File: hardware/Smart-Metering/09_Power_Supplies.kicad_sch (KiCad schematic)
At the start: 36 parts, among them J901 BATTERY_1S, SW901 POWER, U901 BQ24074RGT, U902 TPS63001, U903 TPS61089

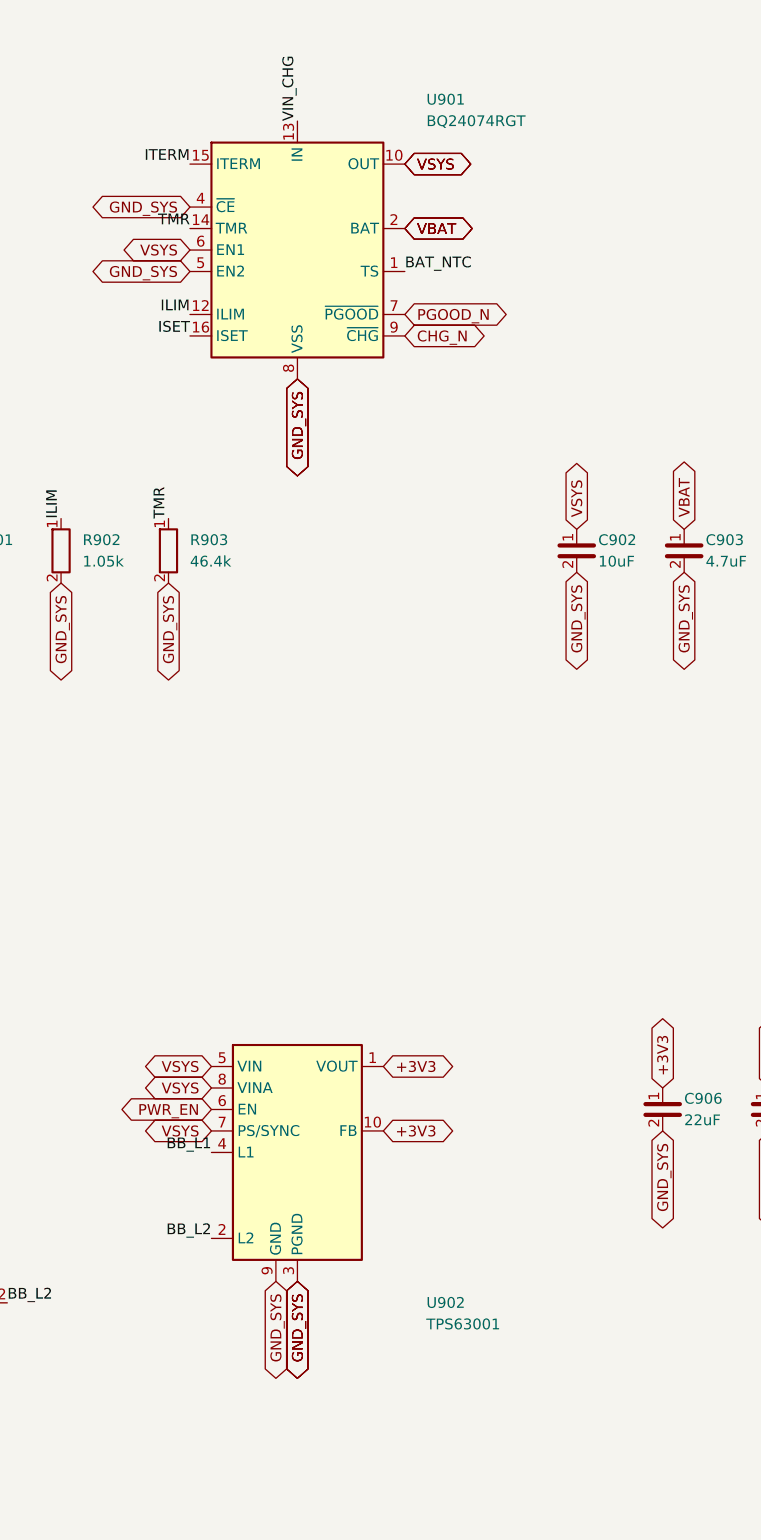
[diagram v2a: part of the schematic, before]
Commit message: Completa o esquemático: MCU, interface HMI e comunicações
05_Metrology_MCU: STM32F413RHT6 (símbolo oficial), mesma família da
plataforma de referência da biblioteca ADSW-PQ-CLS (NUCLEO-F413ZH).
SPI1 isolado para ADE9430/MCP3204, IRQ/DREADY/ZX em EXTI, CF1/CF2 em
timers, USART2 para a HMI, USART3 + DE para RS-485, USB FS, VBAT_SENSE,
estado do carregador, HSE 8 MHz, RTC com LSE 32,768 kHz e CR2032, SWD
de 10 pinos e LEDs de status e pulso.

07_HMI_Interface: conector J701 para a placa HMI (ESP32-P4), com +5V
protegido por PTC e UART/IRQ/EN com resistores de 33 Ω.

08_Communications: RS-485/Modbus isolada com ADM2587E (terminação por
jumper e TVS) e USB-C de serviço com CC de 5,1 kΩ, ESD USBLC6-2SC6 e
detecção de VBUS.

Gerador: direção dos labels pela orientação do pino, pinos empilhados
tratados como um ponto, flags de não conectado.
README e ARCHITECTURE atualizados com o estado completo.

Co-Authored-By: Claude Opus 5.5 <noreply@anthropic.com>
Claude-Session: https://claude.ai/code/session_012B8cVkhtjf3eg98UdpNCpf
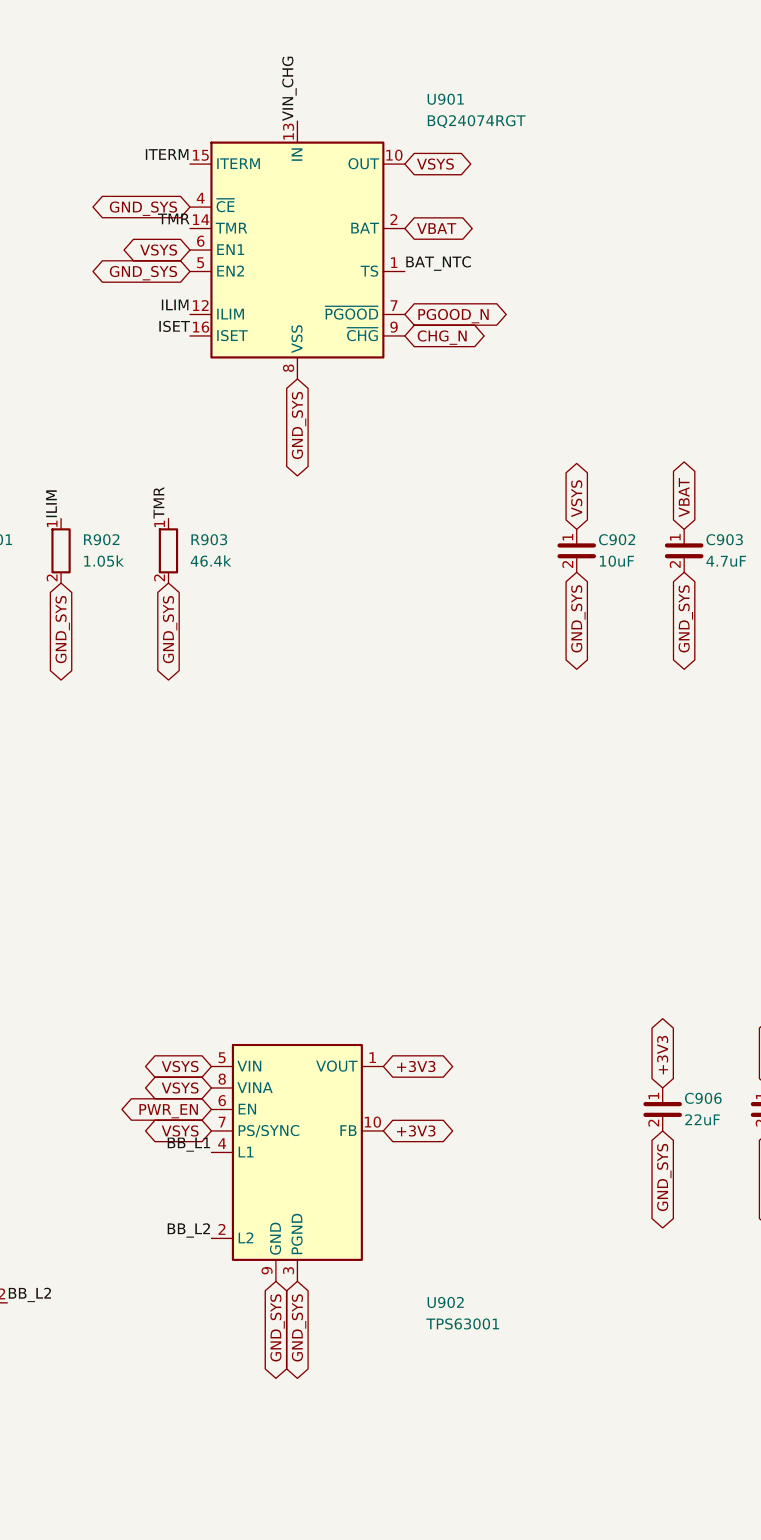
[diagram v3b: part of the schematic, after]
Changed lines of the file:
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@@
 		(property "Intersheetrefs" "${INTERSHEET_REFS}" (at 152.4 55.88 0) (hide yes) (effects (font (size 1.27 1.27))))
-	)
-	(global_label "VSYS" (shape bidirectional) (at 152.4 55.88 0)
-		(effects (font (size 1.27 1.27)) (justify left))
-		(property "Intersheetrefs" "${INTERSHEET_REFS}" (at 152.4 55.88 0) (hide yes) (effects (font (size 1.27 1.27))))
-	)
-	(global_label "VBAT" (shape bidirectional) (at 152.4 63.5 0)
-		(effects (font (size 1.27 1.27)) (justify left))
-		(property "Intersheetrefs" "${INTERSHEET_REFS}" (at 152.4 63.5 0) (hide yes) (effects (font (size 1.27 1.27))))
 	)
 	(global_label "VBAT" (shape bidirectional) (at 152.4 63.5 0)
@@
 		(effects (font (size 1.27 1.27)) (justify left))
 		(property "Intersheetrefs" "${INTERSHEET_REFS}" (at 152.4 76.2 0) (hide yes) (effects (font (size 1.27 1.27))))
-	)
-	(global_label "GND_SYS" (shape bidirectional) (at 139.7 81.28 270)
-		(effects (font (size 1.27 1.27)) (justify right))
-		(property "Intersheetrefs" "${INTERSHEET_REFS}" (at 139.7 81.28 0) (hide yes) (effects (font (size 1.27 1.27))))
 	)
 	(global_label "GND_SYS" (shape bidirectional) (at 139.7 81.28 270)
@@
 	)
 	(global_label "GND_SYS" (shape bidirectional) (at 139.7 187.96 270)
-		(effects (font (size 1.27 1.27)) (justify right))
-		(property "Intersheetrefs" "${INTERSHEET_REFS}" (at 139.7 187.96 0) (hide yes) (effects (font (size 1.27 1.27))))
-	)
-	(global_label "GND_SYS" (shape bidirectional) (at 139.7 187.96 270)

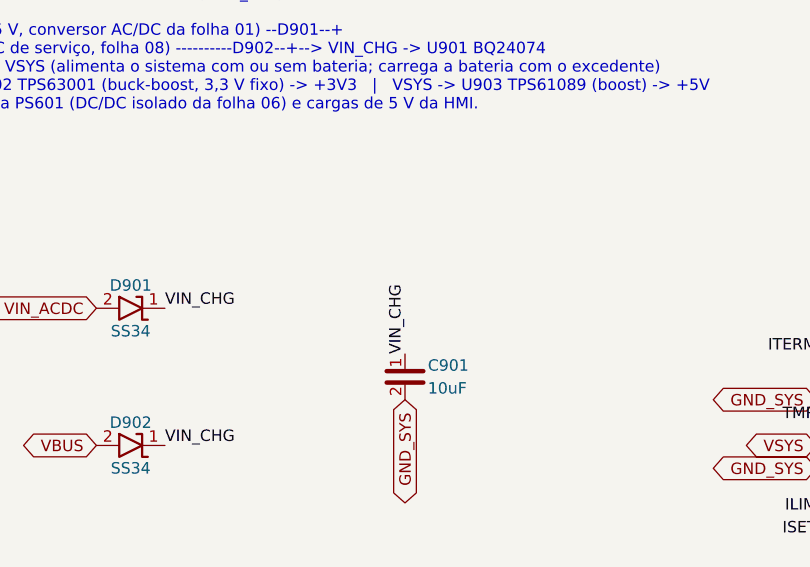
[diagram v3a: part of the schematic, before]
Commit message: Revisão completa do esquemático e correções
Verificação automática sobre o netlist global (215 componentes, 176 nets):
sem pinos soltos, sem nets de alimentação sem fonte, sem saídas em
conflito e isolação íntegra (terras só se encontram nas barreiras
PS101, PS601, U601, U602 e U801).

Correções:
- footprint do ADE9430 inexistente na biblioteca KiCad trocado por
  QFN-40 6x6 (tamanho do pad exposto a confirmar);
- MISO do ADE9430 como tri-state (barramento compartilhado com MCP3204);
- PS101 com símbolo e footprint oficiais do IRM-10-5 (o símbolo genérico
  tinha AC/L e AC/N trocados);
- PWR_FLAG em HV_DC, HV_RTN, VBAT_RTC, VDDA, GND_485 e VIN_CHG;
- footprints para fusíveis, varistores, indutores e chave de energia;
- polarização de fail-safe opcional no RS-485 (R807/R808, DNP);
- notas de layout (retorno do AC/DC) e de firmware (VBUS no PA9).

Relatório com revisão por folha, orçamento de potência e pendências em
docs/REVISAO_ESQUEMATICO.md.

Co-Authored-By: Claude Opus 5.5 <noreply@anthropic.com>
Claude-Session: https://claude.ai/code/session_012B8cVkhtjf3eg98UdpNCpf
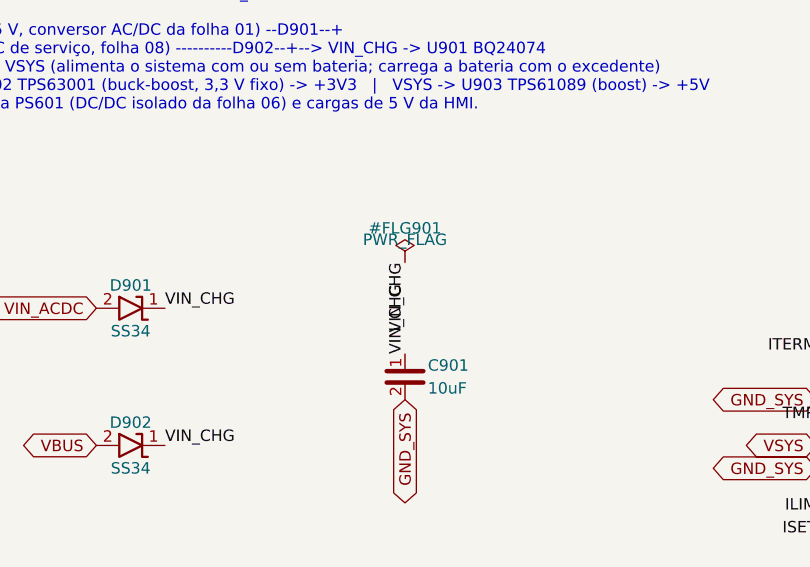
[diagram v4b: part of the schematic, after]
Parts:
- L901: footprint (none) -> Inductor_SMD:L_Bourns-SRN4018
- L902: footprint (none) -> Inductor_SMD:L_Bourns_SRP7028A_7.3x6.6mm
- SW901: footprint (none) -> Connector_JST:JST_PH_B2B-PH-K_1x02_P2.00mm_Vertical
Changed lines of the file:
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@@
 		(property "Intersheetrefs" "${INTERSHEET_REFS}" (at 54.61 127 0) (hide yes) (effects (font (size 1.27 1.27))))
+	)
+	(label "VIN_CHG" (at 81.28 45.72 270)
+		(effects (font (size 1.27 1.27)) (justify right bottom))
 	)
 	(global_label "VSYS" (shape bidirectional) (at 129.54 162.56 180)
@@
 		(property "Reference" "SW901" (at 50.8 124.46 0) (effects (font (size 1.27 1.27))))
 		(property "Value" "POWER" (at 50.8 129.54 0) (effects (font (size 1.27 1.27))))
-		(property "Footprint" "" (at 50.8 127 0) (effects (font (size 1.27 1.27)) (hide yes)))
+		(property "Footprint" "Connector_JST:JST_PH_B2B-PH-K_1x02_P2.00mm_Vertical" (at 50.8 127 0) (effects (font (size 1.27 1.27)) (hide yes)))
 		(property "Datasheet" "" (at 50.8 127 0) (effects (font (size 1.27 1.27)) (hide yes)))
-		(property "Description" "Power switch: closed = converters off" (at 50.8 127 0) (effects (font (size 1.27 1.27)) (hide yes)))
+		(property "Description" "Panel power switch via 2-pin JST: closed = converters off" (at 50.8 127 0) (effects (font (size 1.27 1.27)) (hide yes)))
 		(pin "1")
 		(pin "2")
@@
 			(project "Smart-Metering"
 				(path "/5fa62d70-4279-48bb-8603-6bcc60fb353a/a10e1009-0009-4e09-9009-000000000009" (reference "SW901") (unit 1))
+			)
+		)
+	)
+	(symbol
+		(lib_id "power:PWR_FLAG")
+		(at 81.28 45.72 0)
+		(unit 1)(body_style 1)
+		(exclude_from_sim no)(in_bom yes)(on_board yes)(in_pos_files yes)(dnp no)
+		(property "Reference" "#FLG901" (at 81.28 41.91 0) (effects (font (size 1.27 1.27))))
+		(property "Value" "PWR_FLAG" (at 81.28 43.18 0) (effects (font (size 1.27 1.27))))
+		(property "Footprint" "" (at 81.28 45.72 0) (effects (font (size 1.27 1.27)) (hide yes)))
+		(property "Datasheet" "" (at 81.28 45.72 0) (effects (font (size 1.27 1.27)) (hide yes)))
+		(property "Description" "" (at 81.28 45.72 0) (effects (font (size 1.27 1.27)) (hide yes)))
+		(pin "1")
+		(instances
+			(project "Smart-Metering"
+				(path "/5fa62d70-4279-48bb-8603-6bcc60fb353a/a10e1009-0009-4e09-9009-000000000009" (reference "#FLG901") (unit 1))
 			)
 		)
@@
 		(property "Reference" "L901" (at 101.6 187.96 0) (effects (font (size 1.27 1.27))))
 		(property "Value" "2.2uH" (at 101.6 193.04 0) (effects (font (size 1.27 1.27))))
-		(property "Footprint" "" (at 101.6 190.5 0) (effects (font (size 1.27 1.27)) (hide yes)))
+		(property "Footprint" "Inductor_SMD:L_Bourns-SRN4018" (at 101.6 190.5 0) (effects (font (size 1.27 1.27)) (hide yes)))
 		(property "Datasheet" "" (at 101.6 190.5 0) (effects (font (size 1.27 1.27)) (hide yes)))
-		(property "Description" "Buck-boost inductor, Isat >= 2.5 A" (at 101.6 190.5 0) (effects (font (size 1.27 1.27)) (hide yes)))
+		(property "Description" "Buck-boost inductor, Isat >= 2.5 A (e.g. Bourns SRN4018-2R2M)" (at 101.6 190.5 0) (effects (font (size 1.27 1.27)) (hide yes)))
 		(pin "1")
 		(pin "2")
@@
 		(property "Reference" "L902" (at 101.6 226.06 0) (effects (font (size 1.27 1.27))))
 		(property "Value" "2.2uH" (at 101.6 231.14 0) (effects (font (size 1.27 1.27))))
-		(property "Footprint" "" (at 101.6 228.6 0) (effects (font (size 1.27 1.27)) (hide yes)))
+		(property "Footprint" "Inductor_SMD:L_Bourns_SRP7028A_7.3x6.6mm" (at 101.6 228.6 0) (effects (font (size 1.27 1.27)) (hide yes)))
 		(property "Datasheet" "" (at 101.6 228.6 0) (effects (font (size 1.27 1.27)) (hide yes)))
-		(property "Description" "Boost inductor, Isat >= 6 A" (at 101.6 228.6 0) (effects (font (size 1.27 1.27)) (hide yes)))
-		(pin "1")
-		(pin "2")
+		(property "Description" "Boost inductor, Isat >= 6 A (e.g. Bourns SRP7028A-2R2M)" (at 101.6 228.6 0) (effects (font (size 1.27 1.27)) (hide yes)))
+		(pin "1")
+		(pin "2")
